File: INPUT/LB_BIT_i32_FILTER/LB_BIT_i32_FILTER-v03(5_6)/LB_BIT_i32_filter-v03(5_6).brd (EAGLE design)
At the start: 21.4 x 37.9 mm, 59 parts

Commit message: Updated licenses
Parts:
- removed U$4: OSHWCREDIT-KORG, LITTLEBITS:OSHWCREDIT-KORG
- added U$2: OSHWCREDIT-KORG, LITTLEBITS:OSHWCREDIT-KORG
- renumbered FRAME1 to U$1
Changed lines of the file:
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@@
 <?xml version="1.0" encoding="utf-8"?>
 <!DOCTYPE eagle SYSTEM "eagle.dtd">
-<eagle version="6.4">
+<eagle version="6.6.0">
 <drawing>
 <settings>
@@
 <layer number="225" name="225bmp" color="26" fill="10" visible="yes" active="yes"/>
 <layer number="226" name="226bmp" color="27" fill="10" visible="yes" active="yes"/>
+<layer number="227" name="227bmp" color="7" fill="1" visible="yes" active="yes"/>
+<layer number="228" name="228bmp" color="7" fill="1" visible="yes" active="yes"/>
 <layer number="248" name="Housing" color="7" fill="1" visible="yes" active="yes"/>
 <layer number="249" name="Edge" color="7" fill="1" visible="yes" active="yes"/>
@@
 <attribute name="VALUE" x="12.357" y="15.984" size="0.4064" layer="28" font="vector" rot="MR90"/>
 </element>
-<element name="FRAME1" library="LITTLEBITS" package="FABDWG01-OHW" value="FRAME-LETTER-OHWOHW" x="0" y="0"/>
 <element name="I32C9" library="LITTLEBITS" package="CAP-0603" value="0.1uF" x="3.6" y="18.2" smashed="yes" rot="MR0">
 <attribute name="LB_PN" value="" x="3.6" y="18.2" size="1.778" layer="28" rot="MR0" display="off"/>
@@
 </element>
 <element name="U$3" library="LITTLEBITS" package="OSHW-LOGO-L" value="OSHW-LOGOL" x="-29.35" y="-65.2"/>
-<element name="U$4" library="LITTLEBITS" package="OSHWCREDIT-KORG" value="OSHWCREDIT-KORG" x="-55.2" y="-72.8"/>
+<element name="U$1" library="LITTLEBITS" package="FABDWG01-OHW" value="FRAME-LETTER-OHWOHW" x="0" y="0"/>
+<element name="U$2" library="LITTLEBITS" package="OSHWCREDIT-KORG" value="OSHWCREDIT-KORG" x="-68.95" y="-72.1"/>
 </elements>
 <signals>

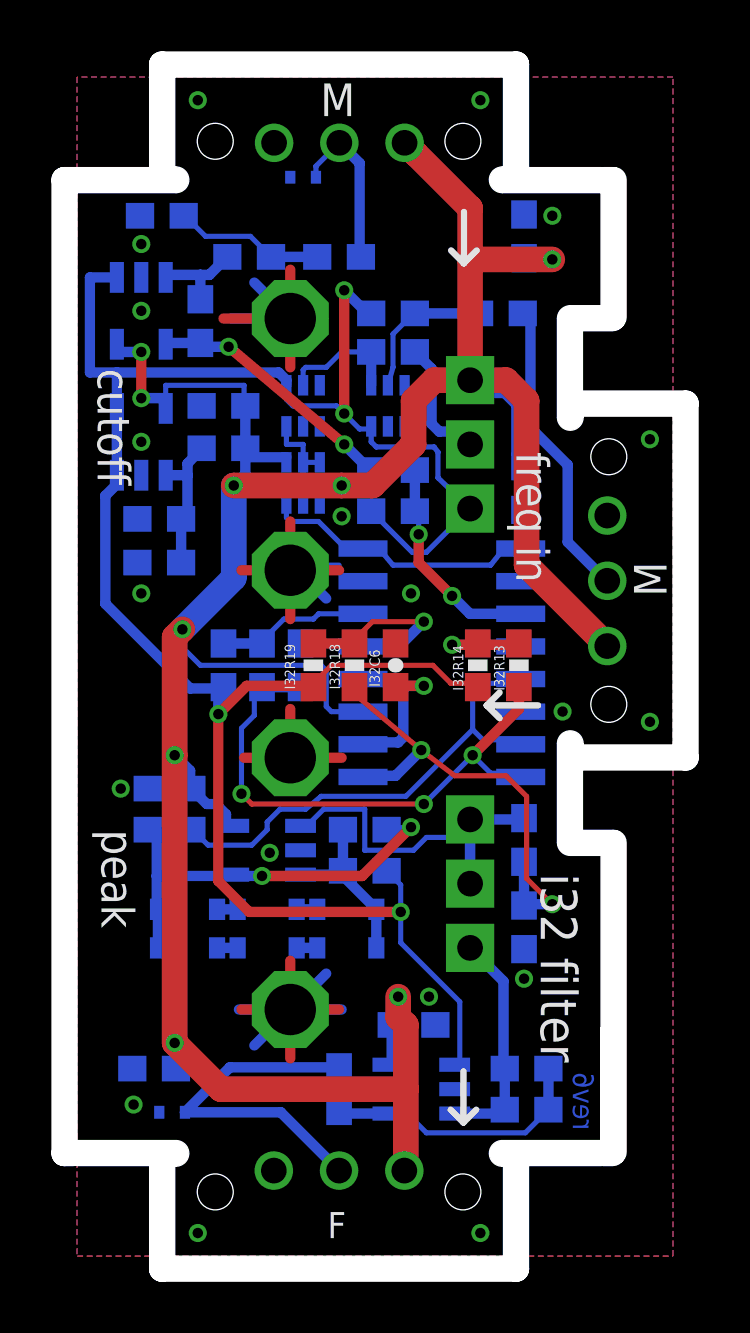
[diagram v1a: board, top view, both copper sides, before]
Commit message: Updated license in Korg bits modules
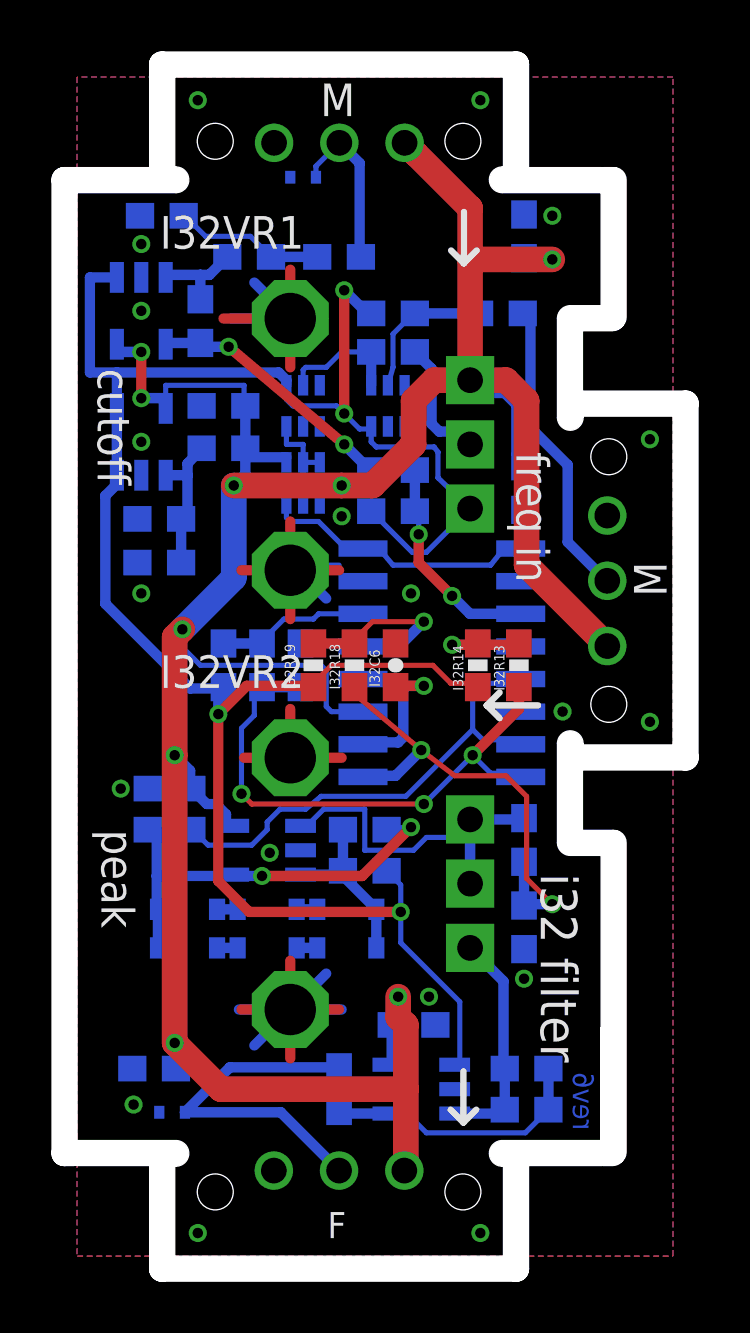
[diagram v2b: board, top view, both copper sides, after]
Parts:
- moved U$2 6.90 mm to (-75.6, -70.2)
- moved U$3 2.88 mm to (-30.9, -67.6)
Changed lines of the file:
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@@
 <layer number="111" name="LB_TEXT" color="13" fill="1" visible="yes" active="yes"/>
 <layer number="112" name="tSilk" color="7" fill="1" visible="yes" active="yes"/>
+<layer number="113" name="ReferenceLS" color="7" fill="1" visible="yes" active="yes"/>
 <layer number="116" name="Patch_BOT" color="9" fill="4" visible="yes" active="yes"/>
+<layer number="118" name="Rect_Pads" color="7" fill="1" visible="yes" active="yes"/>
 <layer number="121" name="_tsilk" color="7" fill="1" visible="yes" active="yes"/>
 <layer number="122" name="_bsilk" color="7" fill="1" visible="yes" active="yes"/>
@@
 <attribute name="LB_PN" value="?" x="8.8" y="42" size="1.778" layer="28" rot="MR180" display="off"/>
 <attribute name="V_OPERATION" value="5V" x="8.8" y="42" size="1.778" layer="28" rot="MR180" display="off"/>
-<attribute name="IEC_ESD_PROT" value="+/-18kV" x="8.8" y="42" size="1.778" layer="28" rot="MR180" display="off"/>
 <attribute name="V_CLAMP" value="?" x="8.8" y="42" size="1.778" layer="28" rot="MR180" display="off"/>
 <attribute name="NAME" x="7.611" y="43.084" size="0.4064" layer="26" rot="MR180"/>
 <attribute name="VALUE" x="6.684" y="43.797" size="0.4064" layer="28" rot="MR180"/>
+<attribute name="MPN" value="ESD9B5.0ST5G" x="8.8" y="42" size="1.778" layer="28" rot="MR180" display="off"/>
+<attribute name="IEC_ESD_PROT0" value="+/-18kV" x="8.8" y="42" size="1.778" layer="28" rot="MR180" display="off"/>
 </element>
 <element name="I32TVS2" library="LITTLEBITS" package="SOD-923" value="ESD9B5.0ST5G" x="3.7" y="5.6" smashed="yes" rot="MR180">
 <attribute name="LB_PN" value="?" x="-2.25" y="0.3" size="1.778" layer="28" rot="MR180" display="off"/>
 <attribute name="V_OPERATION" value="5V" x="-2.25" y="0.3" size="1.778" layer="28" rot="MR180" display="off"/>
-<attribute name="IEC_ESD_PROT" value="+/-18kV" x="-2.25" y="0.3" size="1.778" layer="28" rot="MR180" display="off"/>
 <attribute name="V_CLAMP" value="?" x="-2.25" y="0.3" size="1.778" layer="28" rot="MR180" display="off"/>
 <attribute name="NAME" x="4.561" y="5.784" size="0.4064" layer="26" rot="MR180"/>
 <attribute name="VALUE" x="1.584" y="5.047" size="0.4064" layer="28" rot="MR180"/>
+<attribute name="MPN" value="ESD9B5.0ST5G" x="3.7" y="5.6" size="1.778" layer="28" rot="MR180" display="off"/>
+<attribute name="IEC_ESD_PROT0" value="+/-18kV" x="3.7" y="5.6" size="1.778" layer="28" rot="MR180" display="off"/>
 </element>
 <element name="I32C3" library="LITTLEBITS" package="CAP-0603" value="0.1uF" x="3" y="7.3" smashed="yes" rot="MR0">
@@
 <attribute name="VALUE" x="2.593" y="19.116" size="0.4064" layer="28" font="vector" rot="MR270"/>
 </element>
-<element name="U$3" library="LITTLEBITS" package="OSHW-LOGO-L" value="OSHW-LOGOL" x="-29.35" y="-65.2"/>
+<element name="U$3" library="LITTLEBITS" package="OSHW-LOGO-L" value="OSHW-LOGOL" x="-30.95" y="-67.6"/>
 <element name="U$1" library="LITTLEBITS" package="FABDWG01-OHW" value="FRAME-LETTER-OHWOHW" x="0" y="0"/>
-<element name="U$2" library="LITTLEBITS" package="OSHWCREDIT-KORG" value="OSHWCREDIT-KORG" x="-68.95" y="-72.1"/>
+<element name="U$2" library="LITTLEBITS" package="OSHWCREDIT-KORG" value="OSHWCREDIT-KORG" x="-75.6" y="-70.25"/>
 </elements>
 <signals>
